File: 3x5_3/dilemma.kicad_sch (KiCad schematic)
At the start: 248 parts, among them J1 USB_C_Receptacle_USB2.0, J102 NA_serial, J105 NA_Conn_01x04_Female, J113 Cirque, J3 NA_GC9A01, J4 Conn_01x05, J5 NA_Conn_01x02, J5001 USB_C_Receptacle_USB2.0, J5002 NA_Conn_01x02, J5003 NA_serial, J5004 NA_GC9A01, J5005 NA_Conn_01x04_Female, J5007 Cirque, J5008 Conn_01x05, J5009 Conn_01x05, J5010 Conn_01x05, SW1 SW_Push, SW101 NA_SW_Push, SW102 NA_SW_Push, SW103 NA_SW_Push, SW104 NA_SW_Push, SW105 NA_SW_Push, SW106 NA_SW_Push, SW107 NA_SW_Push, SW108 NA_SW_Push, SW109 NA_SW_Push, SW112 NA_SW_Push, SW113 NA_SW_Push, SW114 NA_SW_Push, SW115 NA_SW_Push, SW116 NA_SW_Push, SW117 NA_SW_Push, SW118 NA_SW_Push, SW119 NA_SW_Push, SW3001 NA_SW_Push, SW3002 NA_RotaryEncoder_Switch, SW5001 SW_Push, SW5002 NA_SW_Push, SW5003 NA_SW_Push, SW5004 NA_SW_Push, SW5005 NA_SW_Push, SW5006 NA_SW_Push, SW5007 NA_SW_Push, SW5008 NA_SW_Push, SW5009 NA_SW_Push, SW5010 NA_SW_Push, SW5011 NA_SW_Push, SW5012 NA_SW_Push, SW5013 NA_SW_Push, SW5014 NA_SW_Push, SW5015 NA_SW_Push, SW5016 NA_SW_Push, SW5017 NA_SW_Push, SW5018 NA_SW_Push, SW5019 NA_SW_Push, SW5020 NA_RotaryEncoder_Switch, SW5021 SW_SPST, SW5022 SW_SPST, U1 RP2040, U2 W25Q128JVS, U3 XC6210B332MR-G, U4 USBLC6-2P6, U5001 XC6210B332MR-G, U5002 RP2040, U5003 USBLC6-2P6, U5004 W25Q128JVS, U5005 USBLC6-2P6, U5006 USBLC6-2P6, Y1 Crystal_GND24, Y5001 Crystal_GND24

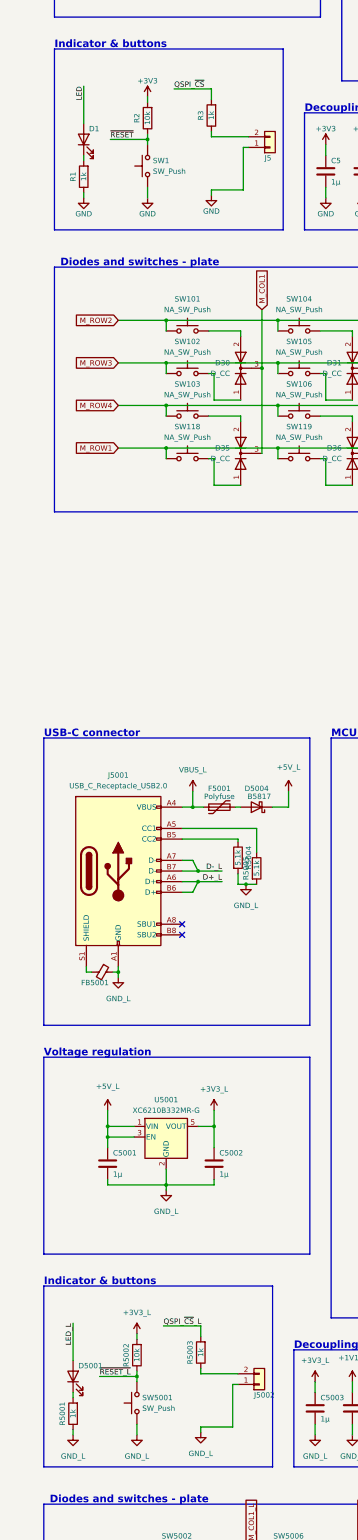
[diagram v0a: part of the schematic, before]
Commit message: flip rst and boot footprints
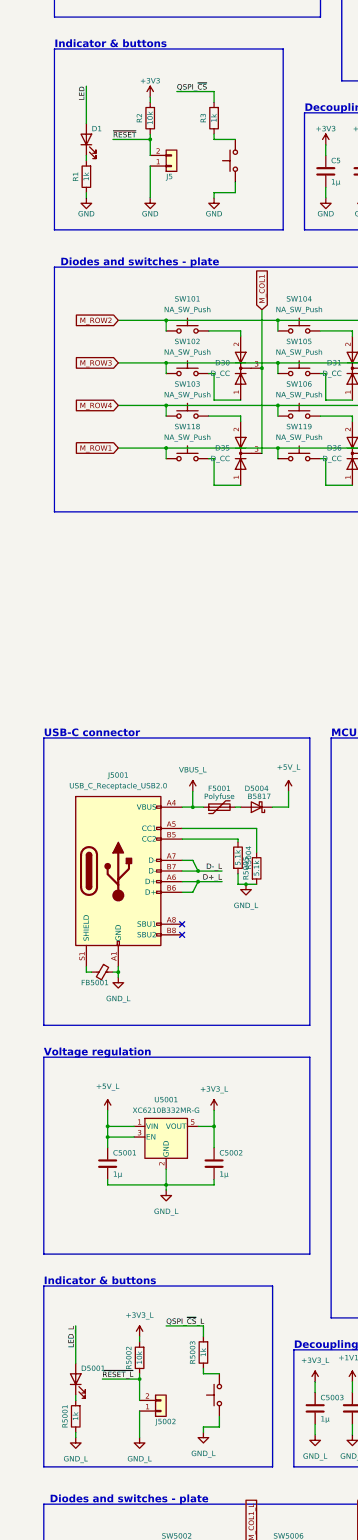
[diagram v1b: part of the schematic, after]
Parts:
- J5, J5002: footprint local-libraries:pinheader_1.27mm_1x02_SMD -> local-libraries:PinHeader_1x02_P1.27mm_Vertical
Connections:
- net ~{RESET_L}: now also J5002.2 (Pin_2); no longer SW5001.2
- net ~{RESET}: now also J5.2 (Pin_2); no longer SW1.2
- net at R3.1: now also SW1.2; no longer J5.2 (Pin_2)
- net at R5003.1: now also SW5001.2; no longer J5002.2 (Pin_2)
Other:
- moved on the sheet: D1, D5001, J5, J5002, R1, R2, R3, R5001, R5002, R5003
